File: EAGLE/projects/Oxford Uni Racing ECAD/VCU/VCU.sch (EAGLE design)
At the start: 71 parts, among them IC2 LM2901D, IC3 4081D, J1 PWR_CAN, J2 ASS+BRAKE_LIGHTS, J3 MC_LEFT, J4 MC_RIGHT, J5 BR_PRESS, J6 LEFT_COOLING_SENSOR, J8 RIGHT_COOLING_SENSOR, K1 RT444012, T2 BT169, U1 REF3040AIDBZT, U3 LMV324, X2 D-SUB9-H2M09ST

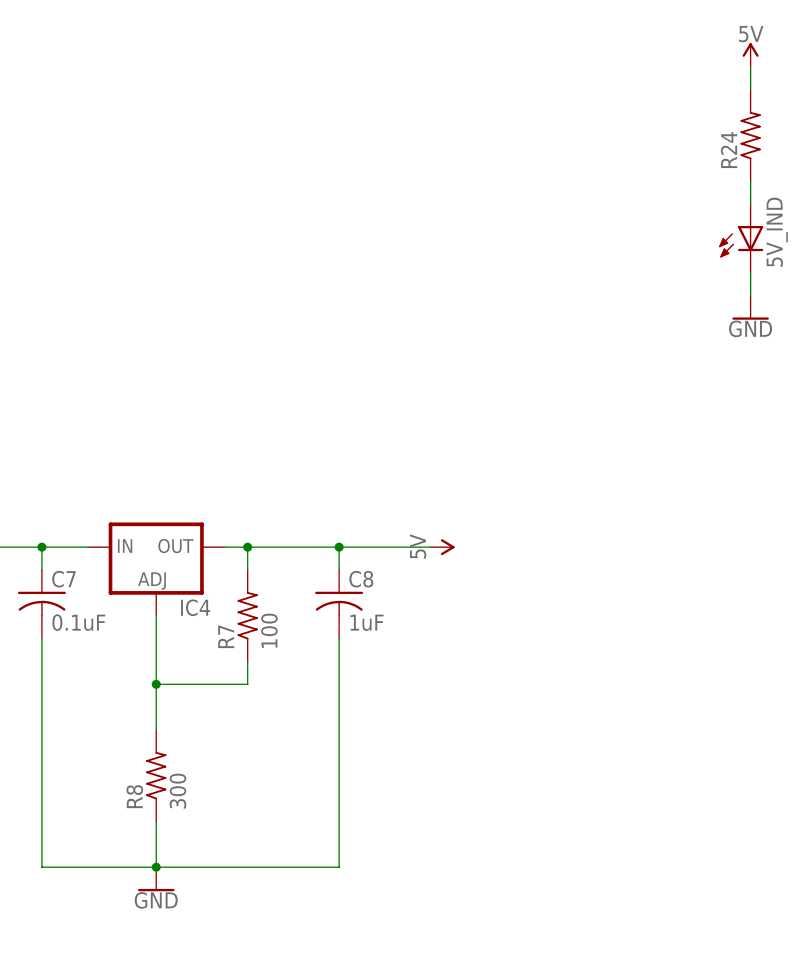
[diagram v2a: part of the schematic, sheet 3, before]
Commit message: replaced resistors with smd
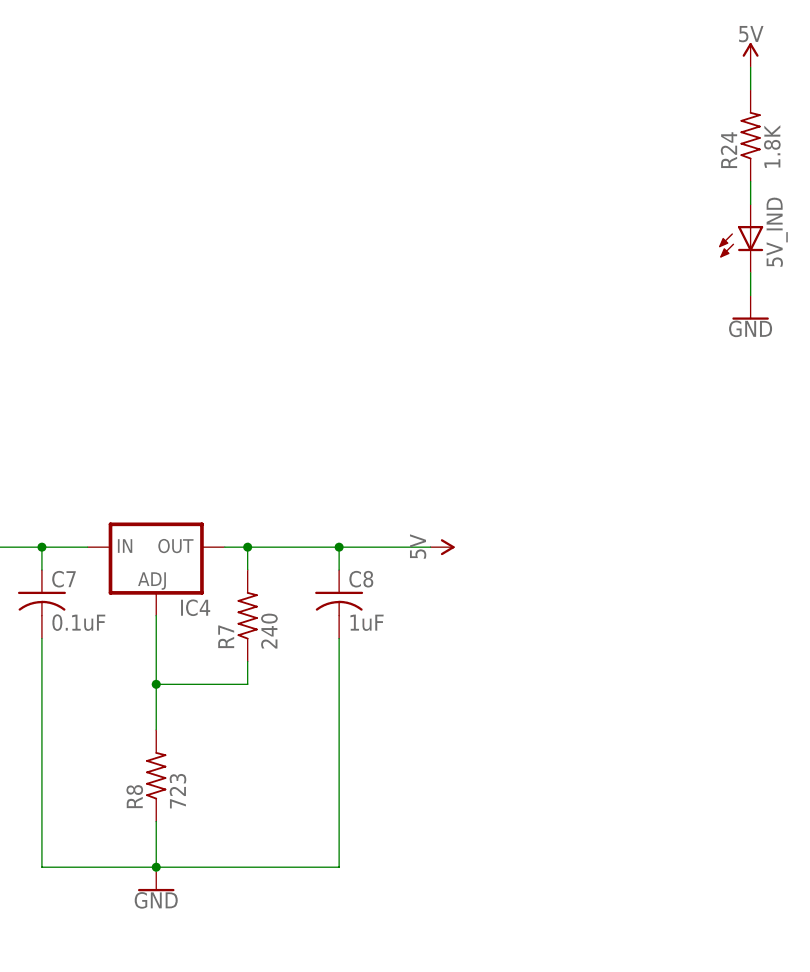
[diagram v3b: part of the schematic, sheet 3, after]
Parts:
- CAN_TERMINATION1: device adafruit:R-US_0204/7 -> adafruit:R-US_R0805
- R24: value (none) -> 1.8K; device adafruit:R-US_0204/7 -> adafruit:R-US_R0805
- R7: value 100 -> 240; device adafruit:R-US_0204/7 -> adafruit:R-US_R0805
- R8: value 300 -> 723; device adafruit:R-US_0204/7 -> adafruit:R-US_R0805
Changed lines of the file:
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@@
 <part name="SUPPLY24" library="SparkFun-PowerSymbols" library_urn="urn:adsk.eagle:library:530" deviceset="12V" device=""/>
 <part name="GND12" library="SparkFun-PowerSymbols" library_urn="urn:adsk.eagle:library:530" deviceset="GND" device=""/>
-<part name="CAN_TERMINATION1" library="adafruit" library_urn="urn:adsk.eagle:library:420" deviceset="R-US_" device="0204/7" package3d_urn="urn:adsk.eagle:package:6240596/1" value="120"/>
+<part name="CAN_TERMINATION1" library="adafruit" library_urn="urn:adsk.eagle:library:420" deviceset="R-US_" device="R0805" package3d_urn="urn:adsk.eagle:package:6240566/1" value="120"/>
 <part name="J1" library="T821108A1S100CEU" deviceset="T821108A1S100CEU" device="" value="PWR_CAN"/>
 <part name="IC4" library="v-reg" library_urn="urn:adsk.eagle:library:409" deviceset="LM317TS" device="" package3d_urn="urn:adsk.eagle:package:30353/1"/>
-<part name="R7" library="adafruit" library_urn="urn:adsk.eagle:library:420" deviceset="R-US_" device="0204/7" package3d_urn="urn:adsk.eagle:package:6240596/1" value="100"/>
-<part name="R8" library="adafruit" library_urn="urn:adsk.eagle:library:420" deviceset="R-US_" device="0204/7" package3d_urn="urn:adsk.eagle:package:6240596/1" value="300"/>
+<part name="R7" library="adafruit" library_urn="urn:adsk.eagle:library:420" deviceset="R-US_" device="R0805" package3d_urn="urn:adsk.eagle:package:6240566/1" value="240"/>
+<part name="R8" library="adafruit" library_urn="urn:adsk.eagle:library:420" deviceset="R-US_" device="R0805" package3d_urn="urn:adsk.eagle:package:6240566/1" value="723"/>
 <part name="C7" library="adafruit" library_urn="urn:adsk.eagle:library:420" deviceset="C-US" device="050-025X075" package3d_urn="urn:adsk.eagle:package:6240357/1" value="0.1uF"/>
 <part name="C8" library="adafruit" library_urn="urn:adsk.eagle:library:420" deviceset="C-US" device="050-025X075" package3d_urn="urn:adsk.eagle:package:6240357/1" value="1uF"/>
@@
 <part name="F1" library="special" library_urn="urn:adsk.eagle:library:367" deviceset="FUSE" device="" package3d_urn="urn:adsk.eagle:package:26650/1" value="1A"/>
 <part name="5V_IND" library="adafruit" library_urn="urn:adsk.eagle:library:420" deviceset="LED" device="3MM" package3d_urn="urn:adsk.eagle:package:6240537/1"/>
-<part name="R24" library="adafruit" library_urn="urn:adsk.eagle:library:420" deviceset="R-US_" device="0204/7" package3d_urn="urn:adsk.eagle:package:6240596/1"/>
+<part name="R24" library="adafruit" library_urn="urn:adsk.eagle:library:420" deviceset="R-US_" device="R0805" package3d_urn="urn:adsk.eagle:package:6240566/1" value="1.8K"/>
 <part name="SUPPLY54" library="SparkFun-PowerSymbols" library_urn="urn:adsk.eagle:library:530" deviceset="5V" device=""/>
 <part name="GND33" library="SparkFun-PowerSymbols" library_urn="urn:adsk.eagle:library:530" deviceset="GND" device=""/>

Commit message: vcu board design done
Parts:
- added AUDIO_OUT_TR: IRLML2502GTRPBF, adafruit:MOSFET-NREFLOW
- added R22: 1K, adafruit:R-US_R0805
- added R23: 47K, adafruit:R-US_R0805
- J1: value PWR_CAN -> Connector A
- J2: value ASS+BRAKE_LIGHTS -> Connector C, D, ii
- J5: value BR_PRESS -> Connector 3
- X1: value (none) -> Connector i
- renumbered BR_LIGHTS_TR to ASS_TRIP
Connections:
- removed net AIR_COILS: J2.8, U$1.J5030-D7
- removed net BATT_CURRENT: IC2A.+IN
- removed net BR_PRESS: IC2B.+IN
- removed net N$16: J8.5, R17.1
- removed net N$18: J8.7, R21.1
- removed net N$20: J6.7, R16.1
- removed net N$22: J6.5, R11.1
- removed net TEMP+_L_OUT: J6.6
- removed net TEMP+_R_OUT: J8.6
- removed net TEMP-_L_OUT: J6.8
- removed net TEMP-_R_OUT: J8.8
- new net AIR_C_1: J2.3, U$1.J50733-D25
- new net AIR_C_2: J2.4, U$1.J50732-D27
- new net AIR_C_3: J2.6, U$1.J5073-D26
- new net AUDIO_OUT: R22.1, U$1.J5030-D7
- new net AUDIO_OUT-: AUDIO_OUT_TR.D, J5.2
- new net CURR_S_SIG: IC2A.+IN, J5.7, U$1.J50713-D46
- new net N$23: AUDIO_OUT_TR.G, R22.2, R23.2
- new net TEMP_L_IN: J6.5, R11.1, U$1.J5027-AD7
- new net TEMP_L_OUT: J6.6, R16.1, U$1.J5025-AD5
- new net TEMP_R_IN: J8.5, R17.1, U$1.J5021-AD1
- new net TEMP_R_OUT: J8.6, R21.1, U$1.J5024-AD4
- new net TSAL_STATE: J2.1, U$1.J5074-D28
- net 12V: now also J5.1
- net 12V_BATTERY: now also J1.4, J1.6; no longer J1.1
- net 5V: now also J5.3, J5.4; no longer J2.7, J5.2
- net BRAKE_LIGHTS+: now also J2.7; no longer J2.5
- net BRAKE_LIGHTS-: now also J2.8; no longer J2.6
- net BRAKE_LIGHTS_OUT: now also U$1.J5008-D9; no longer U$1.J5009-D8
- net BR_PRESS_2: now also IC2B.+IN, U$1.J5026-AD6; no longer U$1.J5040-AD8
- net BR_PRESS_2_UNREG: now also J5.8; no longer J5.6
- net CANH: no longer J1.7
- net CANL: now also J1.7; no longer J1.5, J1.6
- net GND: now also AUDIO_OUT_TR.S, J1.1, J1.5, J2.5, J5.5, J5.6, J6.7, J6.8, J8.7, J8.8, R23.1; no longer J1.4, J5.4
- net PRESSURE_L_SIG_IN: now also U$1.J5072-D24
- net PRESSURE_L_SIG_OUT: now also U$1.J50734-D23
- net PRESSURE_R_SIG_IN: now also R3.2, R4.1, U$1.J5023-AD3; no longer R10.1, R9.2
- net PRESSURE_R_SIG_IN_UNREG: now also U3G4.+IN; no longer U3G2.+IN
- net PRESSURE_R_SIG_OUT: now also R10.1, R9.2, U$1.J5022-AD2; no longer R3.2, R4.1
- net PRESSURE_R_SIG_OUT_UNREG: now also U3G2.+IN; no longer U3G4.+IN
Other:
- note added: "AIR_C_SUPPLY"
- note added: "AUDIO_OUT+"
- note added: "BR_PRESS_2_5V"
- note added: "BR_PRESS_2_GND"
- note added: "CURR_SENS_5V"
- note added: "CURR_SENS_GND"
- note added: "TEMP+_L_OUT"
- note added: "TEMP+_R_OUT"
- note added: "TEMP-_L_OUT"
- note added: "TEMP-_R_OUT"
- note removed: "AIR_COILS_SUPPLY"
- moved on the sheet: CAN_TERMINATION1, J6, J8, R11, R16, R17, R21

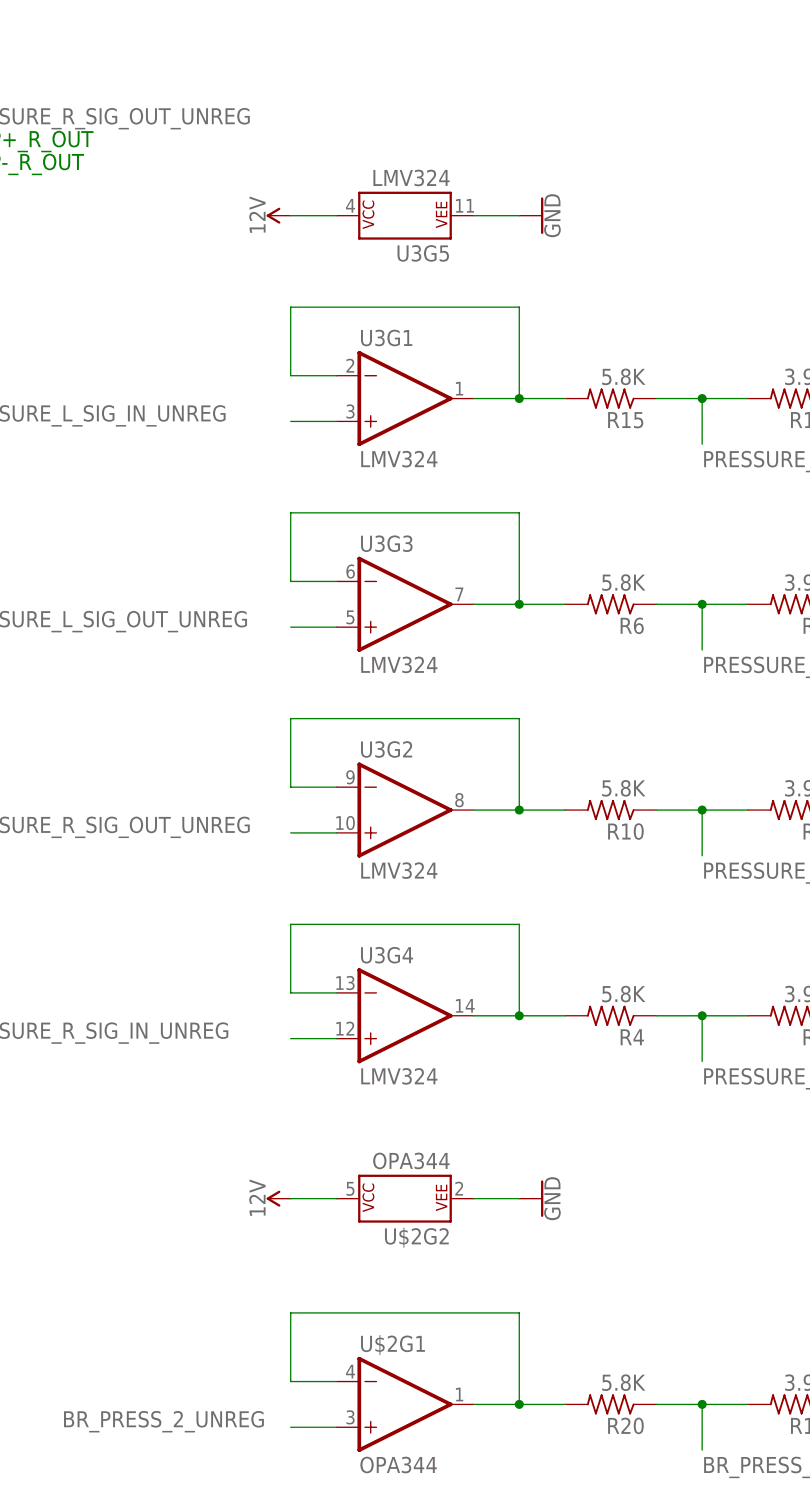
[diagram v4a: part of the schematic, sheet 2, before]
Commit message: added decoupling capacitors
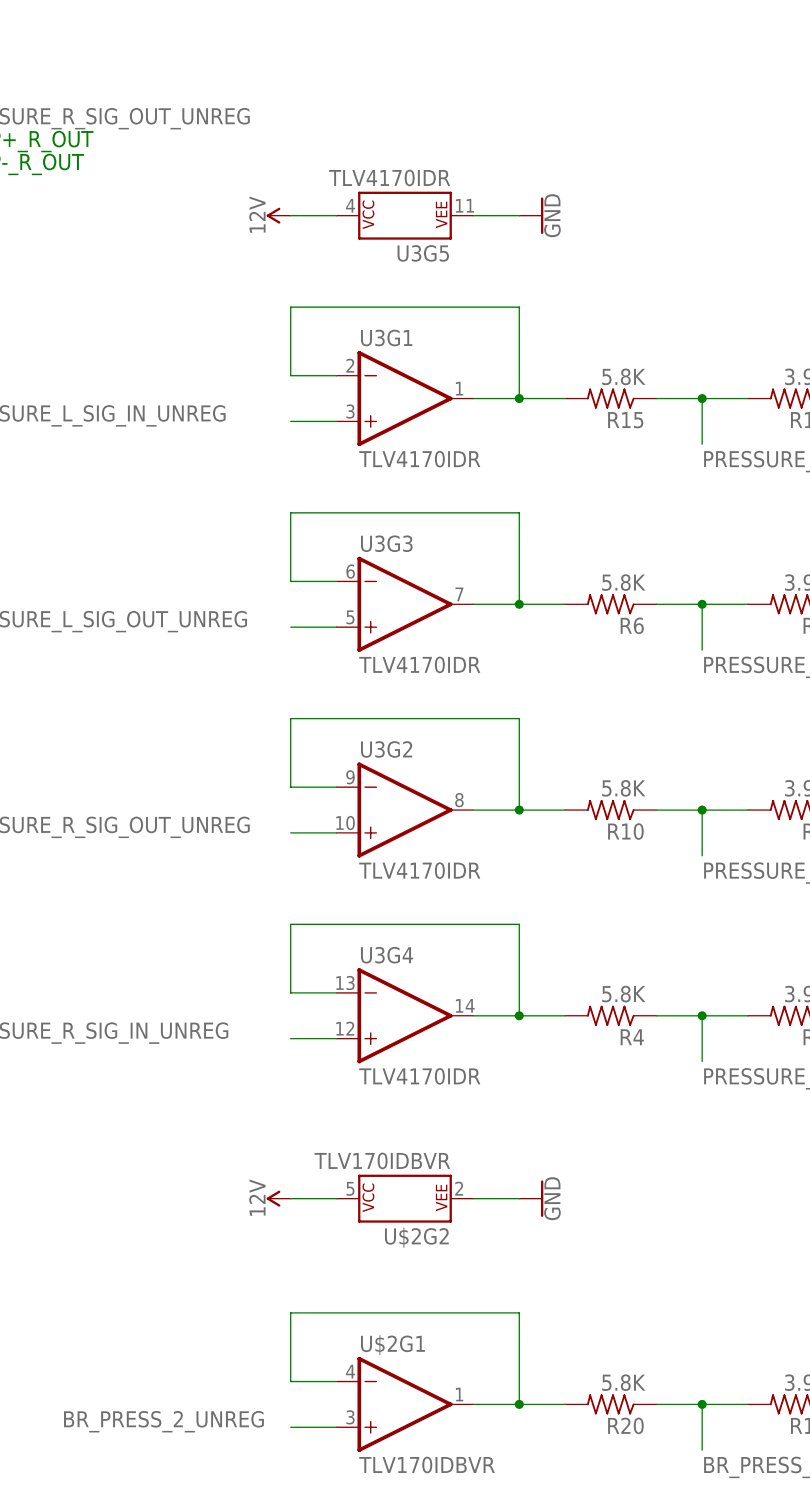
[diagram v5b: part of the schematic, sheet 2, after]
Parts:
- U$2: value OPA344 -> TLV170IDBVR
- U3: value LMV324 -> TLV4170IDR
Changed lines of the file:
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@@
 <part name="SUPPLY19" library="SparkFun-PowerSymbols" library_urn="urn:adsk.eagle:library:530" deviceset="5V" device=""/>
 <part name="SUPPLY37" library="SparkFun-PowerSymbols" library_urn="urn:adsk.eagle:library:530" deviceset="5V" device=""/>
-<part name="U3" library="SparkFun-IC-Amplifiers" library_urn="urn:adsk.eagle:library:520" deviceset="LMV324" device="" package3d_urn="urn:adsk.eagle:package:38668/1" value="LMV324"/>
-<part name="U$2" library="SparkFun-IC-Amplifiers" library_urn="urn:adsk.eagle:library:520" deviceset="OPA344" device="" package3d_urn="urn:adsk.eagle:package:38670/1" value="OPA344"/>
+<part name="U3" library="SparkFun-IC-Amplifiers" library_urn="urn:adsk.eagle:library:520" deviceset="LMV324" device="" package3d_urn="urn:adsk.eagle:package:38668/1" value="TLV4170IDR"/>
+<part name="U$2" library="SparkFun-IC-Amplifiers" library_urn="urn:adsk.eagle:library:520" deviceset="OPA344" device="" package3d_urn="urn:adsk.eagle:package:38670/1" value="TLV170IDBVR"/>
 <part name="SUPPLY38" library="SparkFun-PowerSymbols" library_urn="urn:adsk.eagle:library:530" deviceset="12V" device=""/>
 <part name="SUPPLY39" library="SparkFun-PowerSymbols" library_urn="urn:adsk.eagle:library:530" deviceset="12V" device=""/>

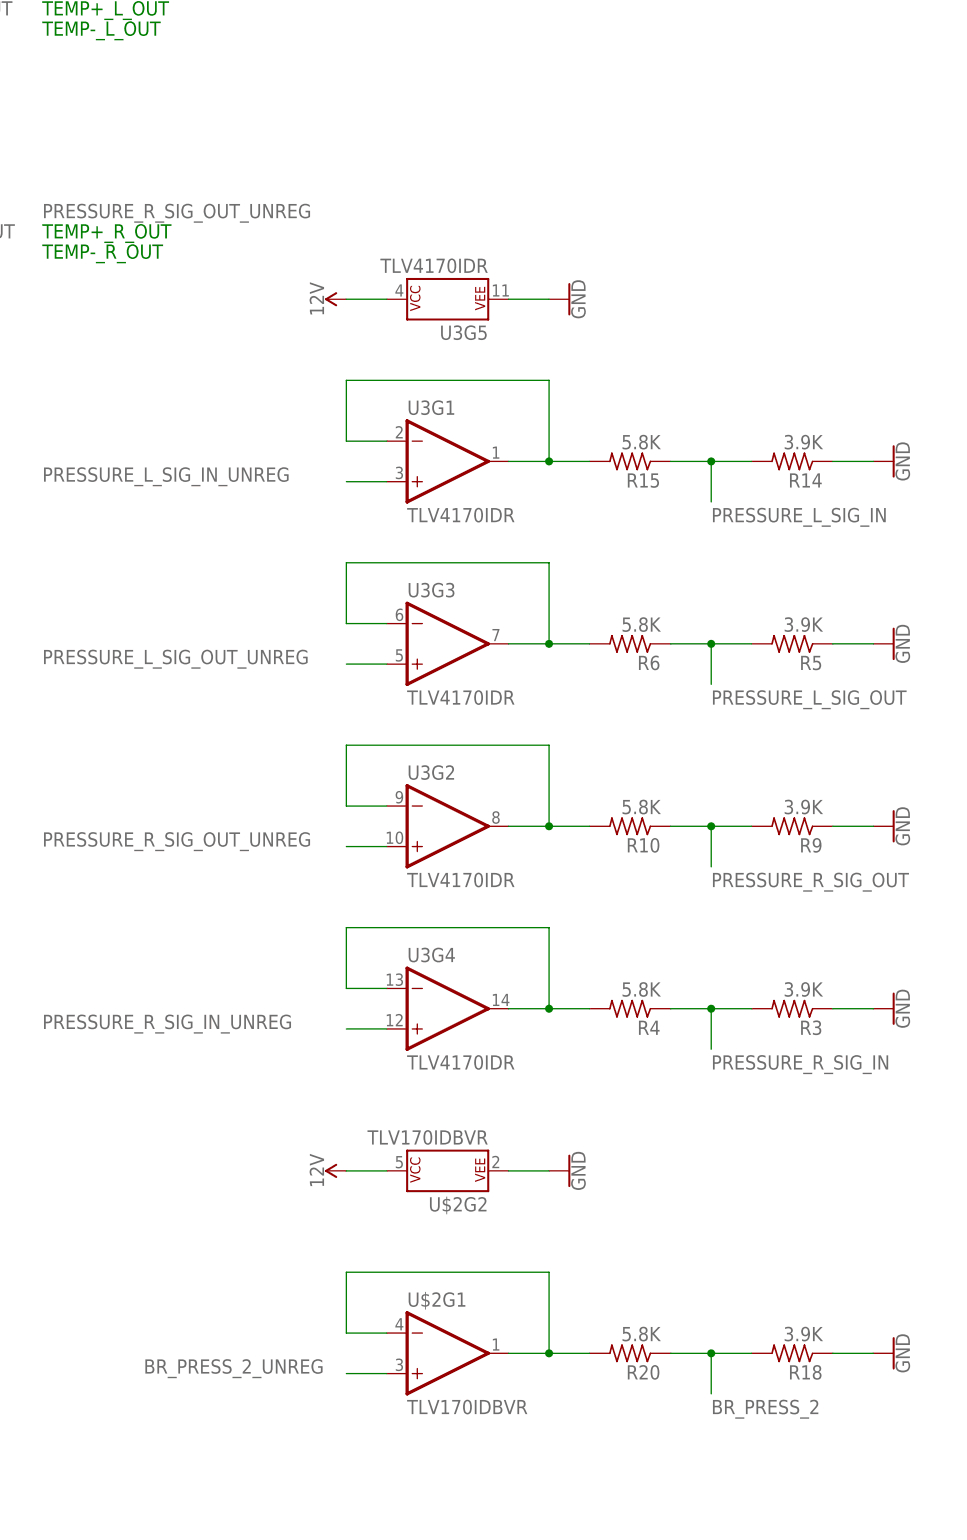
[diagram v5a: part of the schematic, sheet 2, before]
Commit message: added decoupling capacitors
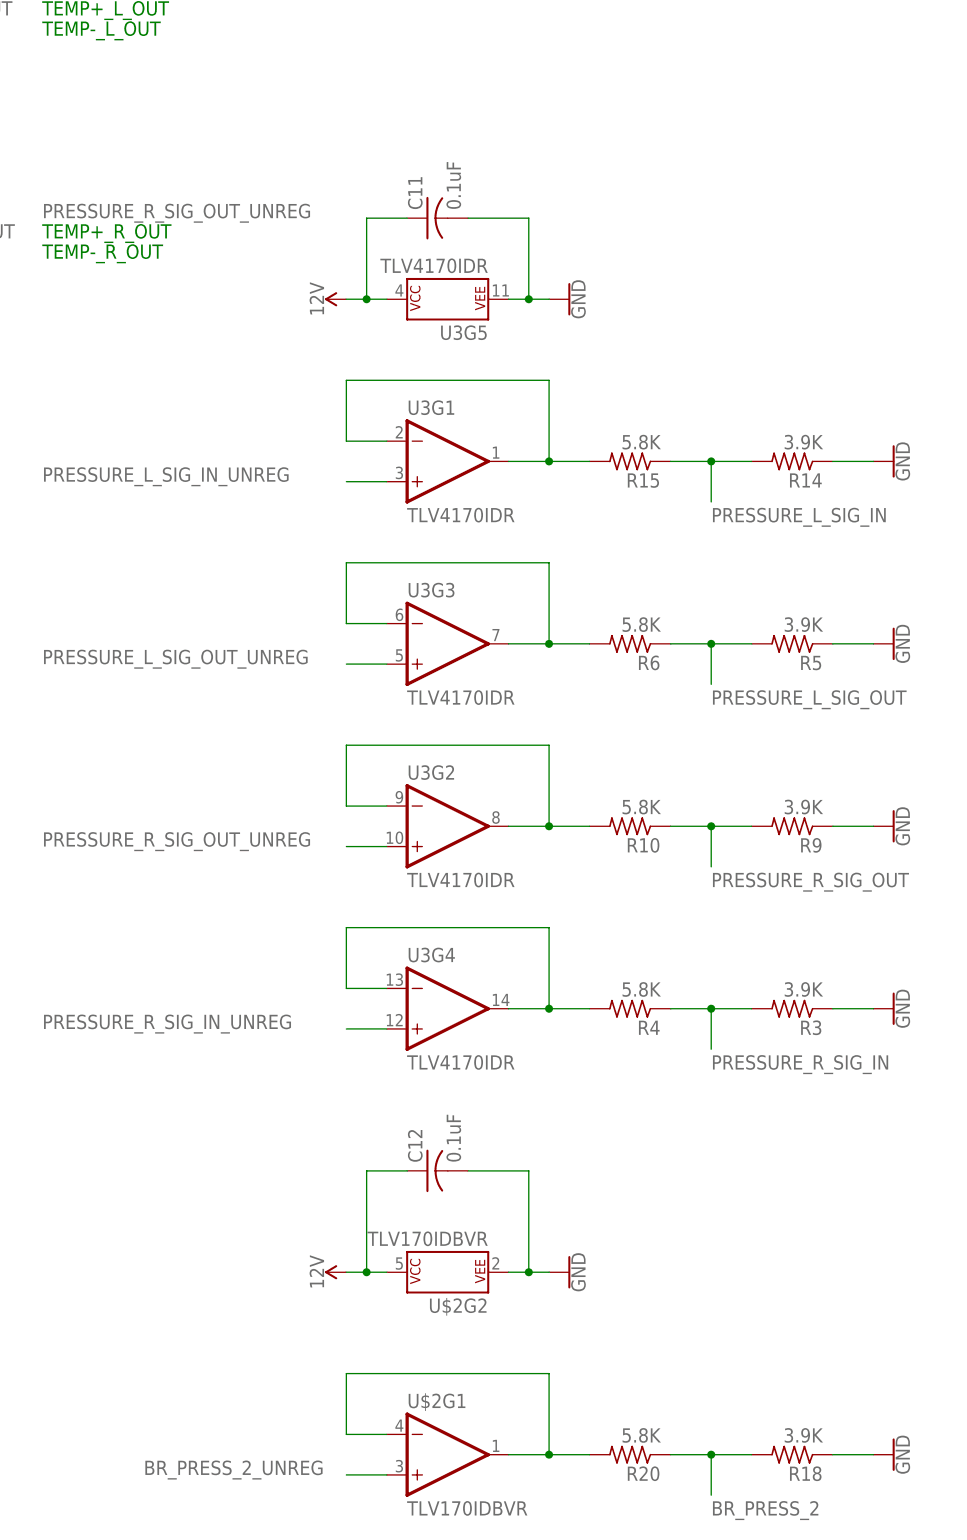
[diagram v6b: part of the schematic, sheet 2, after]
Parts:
- added C11, C12: 0.1uF, adafruit:C-US050-024X044
- added C13: 0.47uF, adafruit:C-US050-024X044
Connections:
- net 12V: now also C11.1, C12.1
- net 5V: now also C13.1
- net GND: now also C11.2, C12.2, C13.2
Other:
- moved on the sheet: R18, R20, U$2G1, U$2G2
